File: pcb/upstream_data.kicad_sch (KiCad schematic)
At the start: 7 parts, among them J6 USB-C data, U12 USBLC6-2SC6

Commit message: specify every capacitor: a rating and a dielectric, chosen from its net
A value on its own is not a specification. Each of the 62 capacitor symbols now carries a voltage
rating and a dielectric picked from the net it sits on -- at least twice the working voltage,
rounded to a standard rating, and never below what a socket the user can reach can present. Both
are hidden fields, so the drawing stays readable and a bill of materials can still be made from it.

Two of the choices are decisions rather than arithmetic.

The connector-side parts are rated for abuse at 50V, because nothing on the board protects them:
both input switches sit downstream of them, so the sink's own supply decoupling and the data
port's see whatever a hostile charger produces with no switch in between.

The charger's input bank is rated 25V on a condition, and the condition is firmware. The input
over-voltage trip defaults to 26V, which is above a 25V part, so rating the bank for its working
voltage is only safe if that trip comes down. The part offers 7V, 12V, 22V and 26V and 12V is the
right one here: the sink never asks for more than 9V, so 12V clears the profile with room and
bounds what the bank can ever see. A board decision that creates a firmware requirement is exactly
the sort that gets lost, so it is recorded on both sides.

What is left open is what the banks are worth once fitted. The charger specifies them as counts of
10uF parts, which only means something if each part is still worth 10uF where it sits, and a
ceramic at 9V is not. The rating and the dielectric are settled; the package is not, and the
package is what decides how much survives. The footprint step has to read each chosen part's bias
curve and add parts if the effective value falls short rather than assume the count was the point.
That is the one piece of this specification that can still change the part count.

Rules check unchanged, and the schematic check is clean.

Co-Authored-By: Claude Opus 5 (1M context) <norepl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
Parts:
- C50: Dielectric (none) -> X7R; Voltage (none) -> 50V
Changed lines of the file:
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@@
+			)
+		)
+		(property "Voltage" "50V"
+			(at 104.14 101.6 0)
+			(show_name no)
+			(do_not_autoplace no)
+			(effects
+				(font
+					(size 1.27 1.27)
+				)
+				(hide yes)
+			)
+		)
+		(property "Dielectric" "X7R"
+			(at 104.14 101.6 0)
+			(show_name no)
+			(do_not_autoplace no)
+			(effects
+				(font
+					(size 1.27 1.27)
+				)
+				(hide yes)
 			)
 		)

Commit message: specify the resistors, and round three values that were never parts
Every resistor now carries a tolerance, and it is 1% only where the value is read: a reference a
part trims itself against, a divider ratio, a termination that states what this end of a cable is,
a value that programs a threshold at power-on. Nineteen of the thirty-eight qualify; the rest are
pull-ups, pull-downs, straps and series parts, where 5% is honest and 1% buys nothing. Power is not
a field, because the largest dissipation anywhere on the board is a few milliwatts in an
indicator's series resistor.

Three values were arithmetic nobody had rounded. 5.24k and 30.31k are the charger vendor's own
calculated figures for the temperature network and neither exists as a part; 172k was ours for the
boost's current limit and is not a standard value either. They become 5.23k, 30.1k and 174k, and
what each costs is recorded: a fraction of a degree on the temperature thresholds, about 2% on the
current limit. A fourth, the hub's reference resistor, had its tolerance written into the value
string; that moves to the field where it belongs.

Reading the boost's datasheet to round the current limit corrected how it had been described. The
limit is not set at the worst-case peak -- the switch has to pass about 4.25A at the bottom of the
cell with every port loaded, so a limit there would trip in normal service. It sits at about 5.9A,
clearing that peak by nearly 40%. The vendor publishes two resistances against measured limits,
which fixes both the relationship and its direction: more resistance, less current.

Rules check unchanged, schematic check clean.

Co-Authored-By: Claude Opus 5 (1M context) <noreply@anthropic.com>
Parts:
- R30, R31, R32, R33: Tolerance (none) -> 1%
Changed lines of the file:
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@@
+			)
+		)
+		(property "Tolerance" "1%"
+			(at 121.92 93.98 0)
+			(show_name no)
+			(do_not_autoplace no)
+			(effects
+				(font
+					(size 1.27 1.27)
+				)
+				(hide yes)
 			)
 		)
@@
 			)
 		)
+		(property "Tolerance" "1%"
+			(at 101.6 111.76 0)
+			(show_name no)
+			(do_not_autoplace no)
+			(effects
+				(font
+					(size 1.27 1.27)
+				)
+				(hide yes)
+			)
+		)
 		(property "Footprint" ""
 			(at 101.6 104.14 0)
@@
 					(size 1.27 1.27)
 				)
+			)
+		)
+		(property "Tolerance" "1%"
+			(at 101.6 114.3 0)
+			(show_name no)
+			(do_not_autoplace no)
+			(effects
+				(font
+					(size 1.27 1.27)
+				)
+				(hide yes)
 			)
 		)
@@
 			)
 		)
+		(property "Tolerance" "1%"
+			(at 121.92 101.6 0)
+			(show_name no)
+			(do_not_autoplace no)
+			(effects
+				(font
+					(size 1.27 1.27)
+				)
+				(hide yes)
+			)
+		)

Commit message: calculate the capacitor banks, and give every one of them a package
The question a value and a rating leave open is how much capacitance is actually there once the
voltage is across it, and the answer differs by package for the same value and rating. So the
requirement is derived bank by bank rather than taken from the vendors' part counts.

The charger's input is the binding case. Holding its input ripple to 100 mV with 5.4 A through the
inductor needs 8.6uF in circuit out of the 20uF fitted, so 43% has to survive 9V. The 5V rail needs
36% of what it carries and the system rail 27%. That last one is worth stating properly: ripple
alone would want only 2.5uF there, so the bank exists to answer load steps, and the realistic fast
step is the radio transmitting and the processor waking rather than the ports, which cannot step
quickly because the boost soft-starts over 4ms. At half an amp over five microseconds that is 25uF
against about 70uF effective.

43% is comfortable in 1206 and marginal in 0603 for a 10uF part at 9V, so the five capacitors on
the 9V nodes take 1206 and everything at 4.5V or under takes 0805. Decoupling goes to 0402, where
being near the pin matters more than the package, and the frequency- and loop-setting parts to
0603, where there is nothing to derate.

The answer to the open item is that the counts do not change: every bank is adequate as drawn
provided each part keeps roughly half of itself, which is what the package choice delivers. What is
left is a purchasing check rather than a design one.

Two asymmetries recorded. The 3.3V converter's vendor states that its recommended values anticipate
tolerance and bias derating and quotes 20% and 50%, so its table is nominal with the margin already
in it; the charger's and the boost's say nothing, so there the derating is ours to carry. And the
processor specifies an effective tolerance rather than a nominal one -- its core regulator's output
capacitor must be 4.7uF +/-20% in circuit.

The checker's 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
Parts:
- C50: footprint (none) -> Capacitor_SMD:C_0402_1005Metric
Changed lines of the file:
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@@
 			)
 		)
-		(property "Footprint" ""
+		(property "Footprint" "Capacitor_SMD:C_0402_1005Metric"
 			(at 104.14 93.98 0)
 			(show_name no)

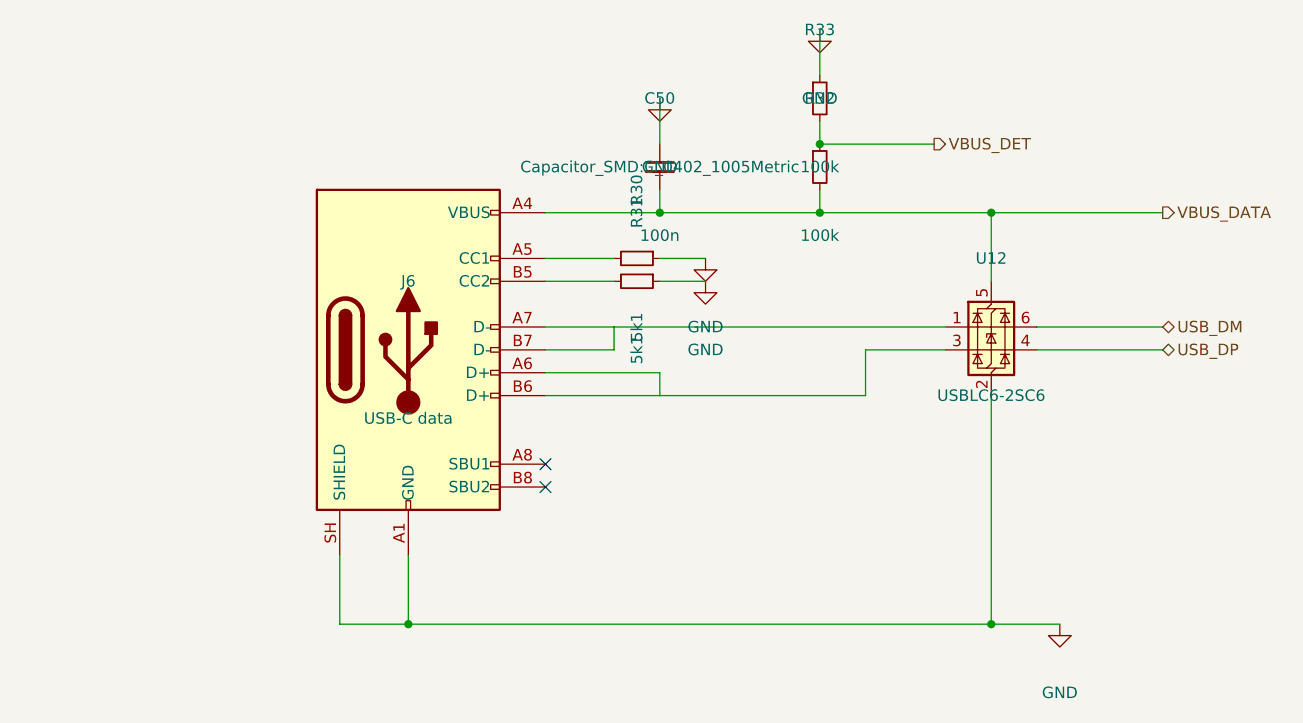
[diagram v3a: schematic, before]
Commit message: assign the footprints, and take the radio module's from its vendor
132 of the 135 parts now carry a footprint. Most follow from the package, the capacitors' follow
from the bias calculation, and the resistors are 0603 rather than 0402 because the board has room,
the first one runs bare on a bench, and a part you can get a probe or an iron onto is worth more
there than the millimetre it saves.

The radio module nearly went in hand-drawn. It has no footprint in any stock library, so the
obvious move was to draw one from the dimension drawing in its datasheet; the pitch, pad size and
pad length read off cleanly, but where each pad sits along its edge did not, and what I had was
inference from where things appeared in a rendered figure rather than a stated number. Raspberry Pi
publish a KiCad symbol and footprint, so that is what is fitted, in a project footprint library
beside the project symbol library. The figure agreed on everything it stated plainly, which says
nothing about the parts it did not.

Taking the official symbol also checked this project's hand-drawn one against theirs. All 21 pins
agree. Four carry different names -- their DI and DO, their nIRQ and WL_ON -- and nothing else
differs, so the pin numbering derived from the module's table is confirmed against its author
rather than merely self-consistent.

Four packages are fitted provisionally and are recorded as such, because what is unsettled about
them is invisible: the processor, the hub, the 3.3V converter and the power sink are in packages
whose library entries differ only in the size of the pad under the part. Body, pitch and pin count
are right; the pad is the nearest variant and wants checking against each vendor's land pattern,
since too small costs thermal performance and too large can wick the part off its pins.

Three parts are deliberately left without one. For the remaining inductors the footprint is the
part -- pad geometry differs between vendors at the same nominal size -- so choosing an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
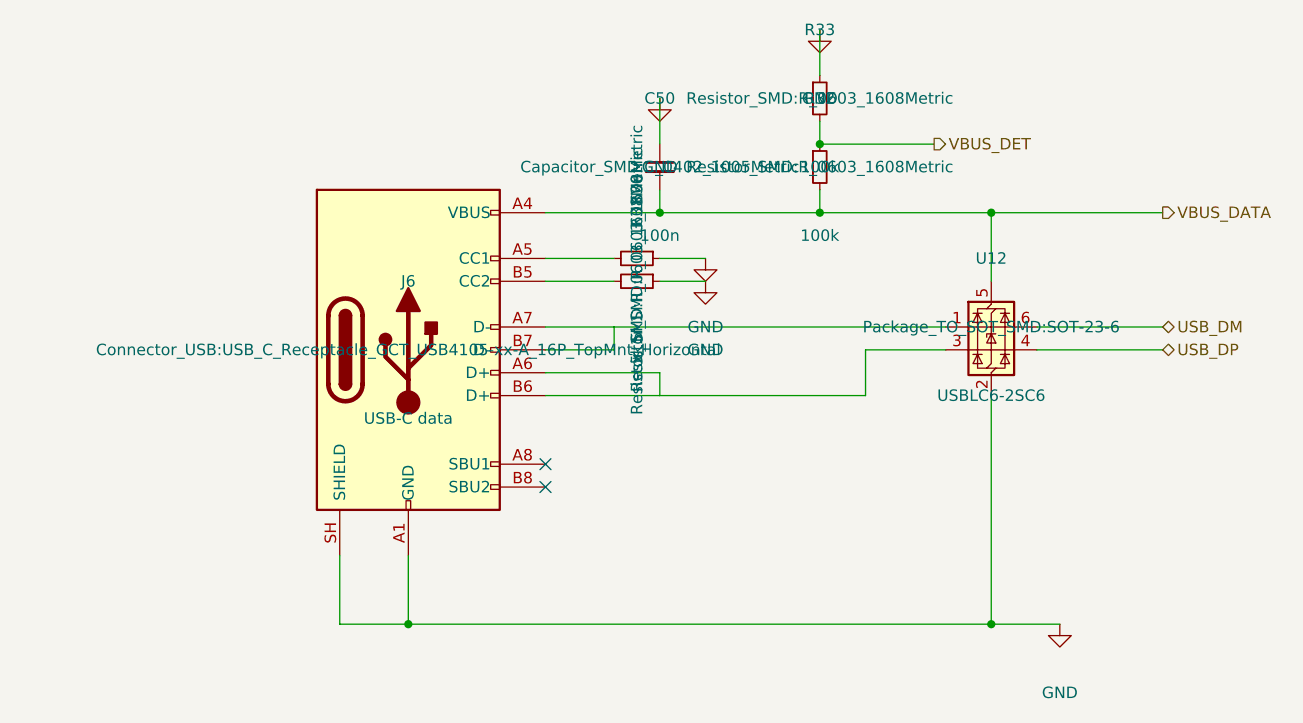
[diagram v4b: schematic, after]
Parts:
- J6: footprint (none) -> Connector_USB:USB_C_Receptacle_GCT_USB4105-xx-A_16P_TopMnt_Horizontal
- R30, R31, R32, R33: footprint (none) -> Resistor_SMD:R_0603_1608Metric
- U12: footprint (none) -> Package_TO_SOT_SMD:SOT-23-6
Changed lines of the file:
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@@
 			)
 		)
-		(property "Footprint" ""
+		(property "Footprint" "Resistor_SMD:R_0603_1608Metric"
 			(at 121.92 86.36 0)
 			(show_name no)
@@
 			)
 		)
-		(property "Footprint" ""
+		(property "Footprint" "Resistor_SMD:R_0603_1608Metric"
 			(at 101.6 104.14 0)
 			(show_name no)
@@
 			)
 		)
-		(property "Footprint" ""
+		(property "Footprint" "Resistor_SMD:R_0603_1608Metric"
 			(at 101.6 106.68 0)
 			(show_name no)
@@
 			)
 		)
-		(property "Footprint" ""
+		(property "Footprint" "Connector_USB:USB_C_Receptacle_GCT_USB4105-xx-A_16P_TopMnt_Horizontal"
 			(at 76.2 114.3 0)
 			(show_name no)
@@
 			)
 		)
-		(property "Footprint" ""
+		(property "Footprint" "Resistor_SMD:R_0603_1608Metric"
 			(at 121.92 93.98 0)
 			(show_name no)
@@
 			)
 		)
-		(property "Footprint" ""
+		(property "Footprint" "Package_TO_SOT_SMD:SOT-23-6"
 			(at 140.97 111.76 0)
 			(show_name no)
